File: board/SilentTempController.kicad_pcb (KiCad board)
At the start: 2 copper layers, 100 x 100 mm, 93 parts, among them J1 Barrel_Jack_Switch, J10 Conn_01x02_Pin, J11 Conn_01x02_Pin, J12 Screw_Terminal_01x02, J13 Screw_Terminal_01x02, J14 Screw_Terminal_01x02, J15 Screw_Terminal_01x02, J2 Screw_Terminal_01x02, J3 Conn_01x02_Pin, J4 Screw_Terminal_01x02, J5 Conn_01x02_Pin, J6 Screw_Terminal_01x02, J7 Conn_01x02_Pin, J8 Screw_Terminal_01x02, J9 Conn_01x02_Pin, Q1 2N3904, Q10 2N3904, Q11 2N3906, Q12 IRLZ44N, Q13 2N3904, Q14 2N3904, Q15 2N3906, Q16 IRLZ44N, Q17 2N3904, Q2 2N3906, Q3 IRLZ44N, Q4 2N3904, Q5 2N3904, Q6 2N3904, Q7 2N3906, Q8 IRLZ44N, Q9 2N3904, SW1 SW_Push, SW2 SW_Push, SW3 SW_Push, SW4 SW_Push, SW5 SW_Push, U1 LM7805_TO220

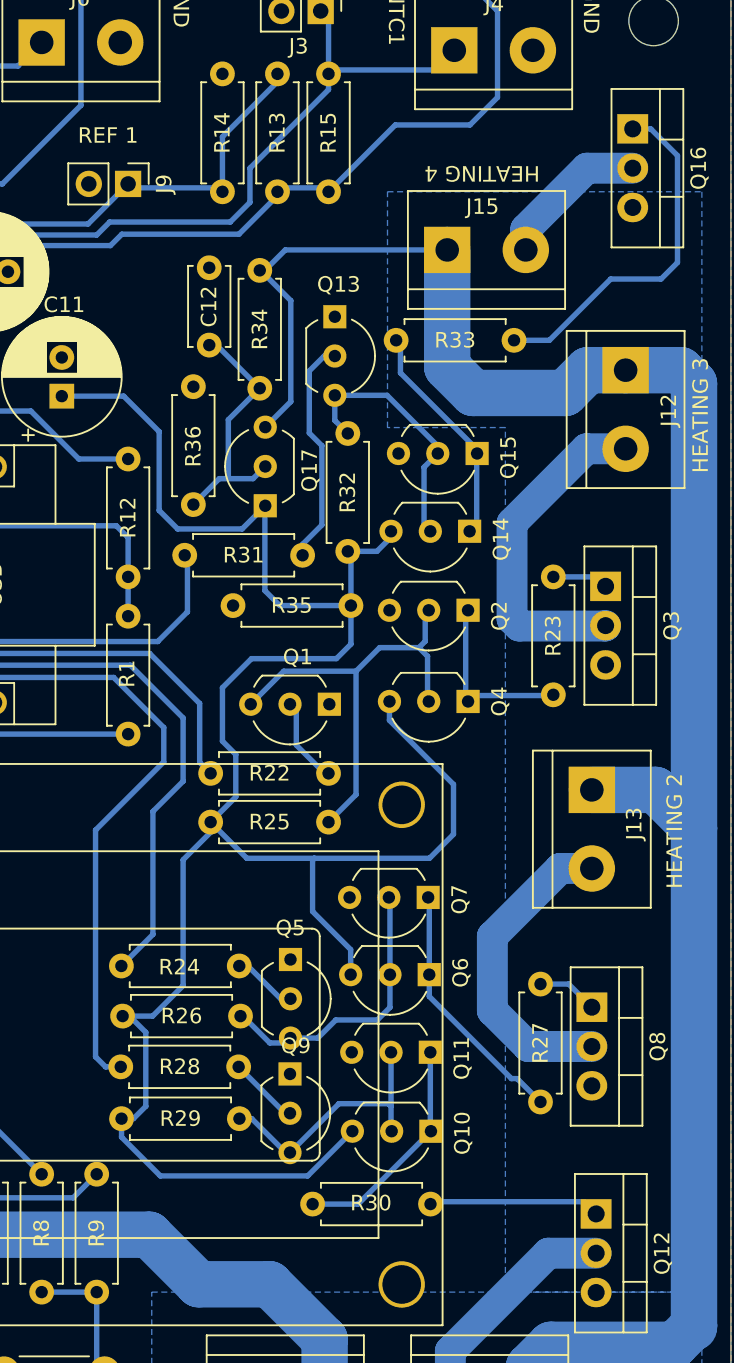
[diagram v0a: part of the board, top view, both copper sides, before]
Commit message: Added snubbers
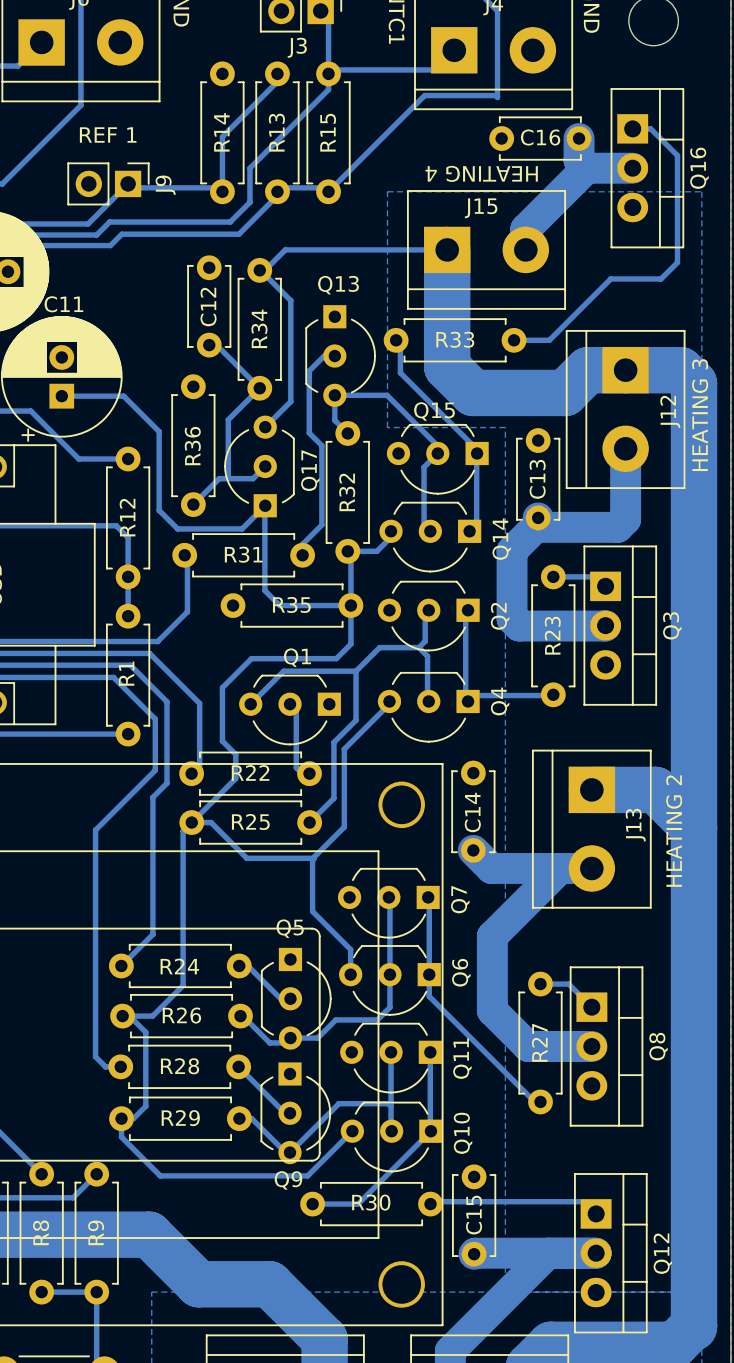
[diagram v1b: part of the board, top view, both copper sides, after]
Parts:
- added C13: 1000 nF, Capacitor_THT:C_Disc_D5.0mm_W2.5mm_P5.00mm, F.Cu at (187.5, 87.1)
- added C14: 1000 nF, Capacitor_THT:C_Disc_D5.0mm_W2.5mm_P5.00mm, F.Cu at (183.3, 108.6)
- added C15: 1000 nF, Capacitor_THT:C_Disc_D5.0mm_W2.5mm_P5.00mm, F.Cu at (183.4, 134.7)
- added C16: 1000 nF, Capacitor_THT:C_Disc_D5.0mm_W2.5mm_P5.00mm, F.Cu at (190.2, 62.6)
- moved R22 1.23 mm to (172.8, 103.7)
- moved R25 1.22 mm to (165.2, 106.8)
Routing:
- net Net-(J13-Pin_2): track 20.4 -> 28.6 mm
- net Net-(J14-Pin_2): track 14.8 -> 22.8 mm
- net +12V: track 140.0 -> 133.4 mm
- net Net-(J12-Pin_2): track 21.8 -> 24.1 mm
- net Net-(J15-Pin_2): track 9.89 -> 12.0 mm
- net /OC1B: track 37.4 -> 36.5 mm
- net Net-(Q1-C): track 29.3 -> 29.8 mm

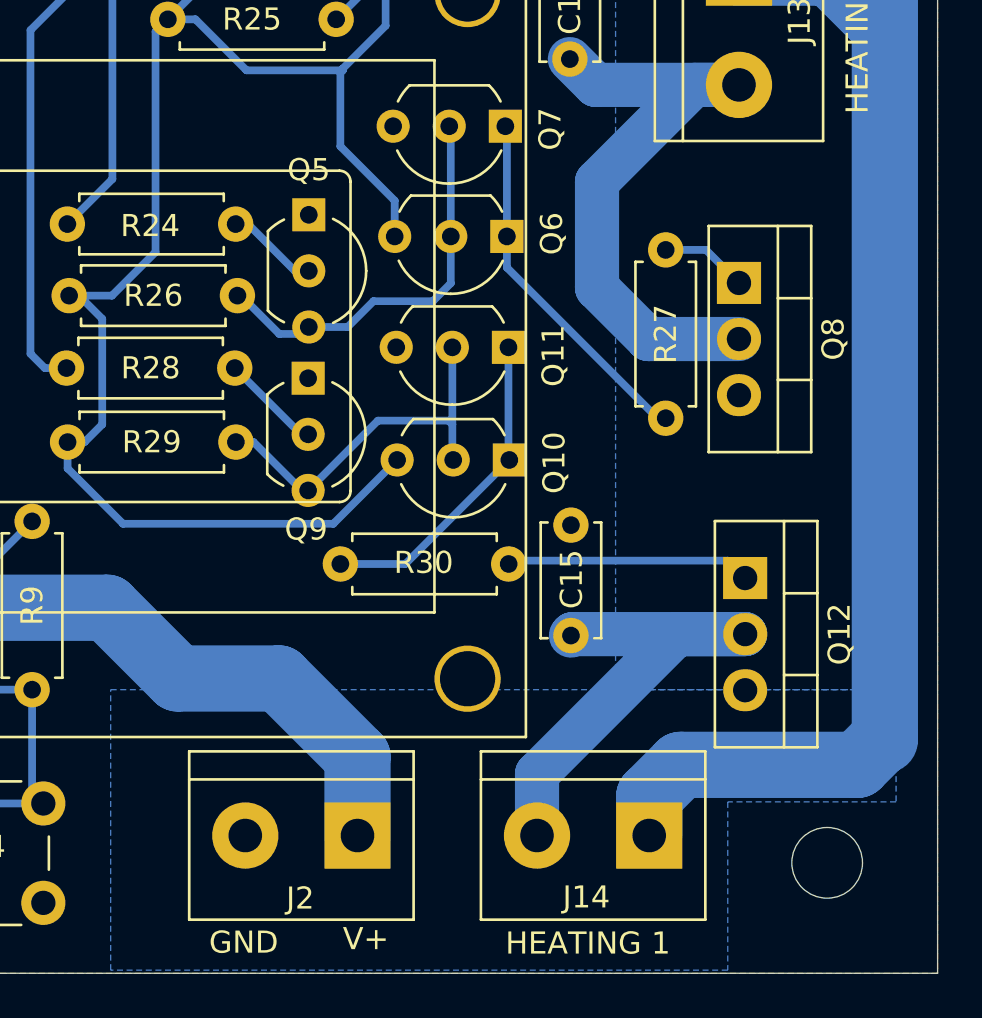
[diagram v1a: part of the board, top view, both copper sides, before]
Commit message: moved connectors
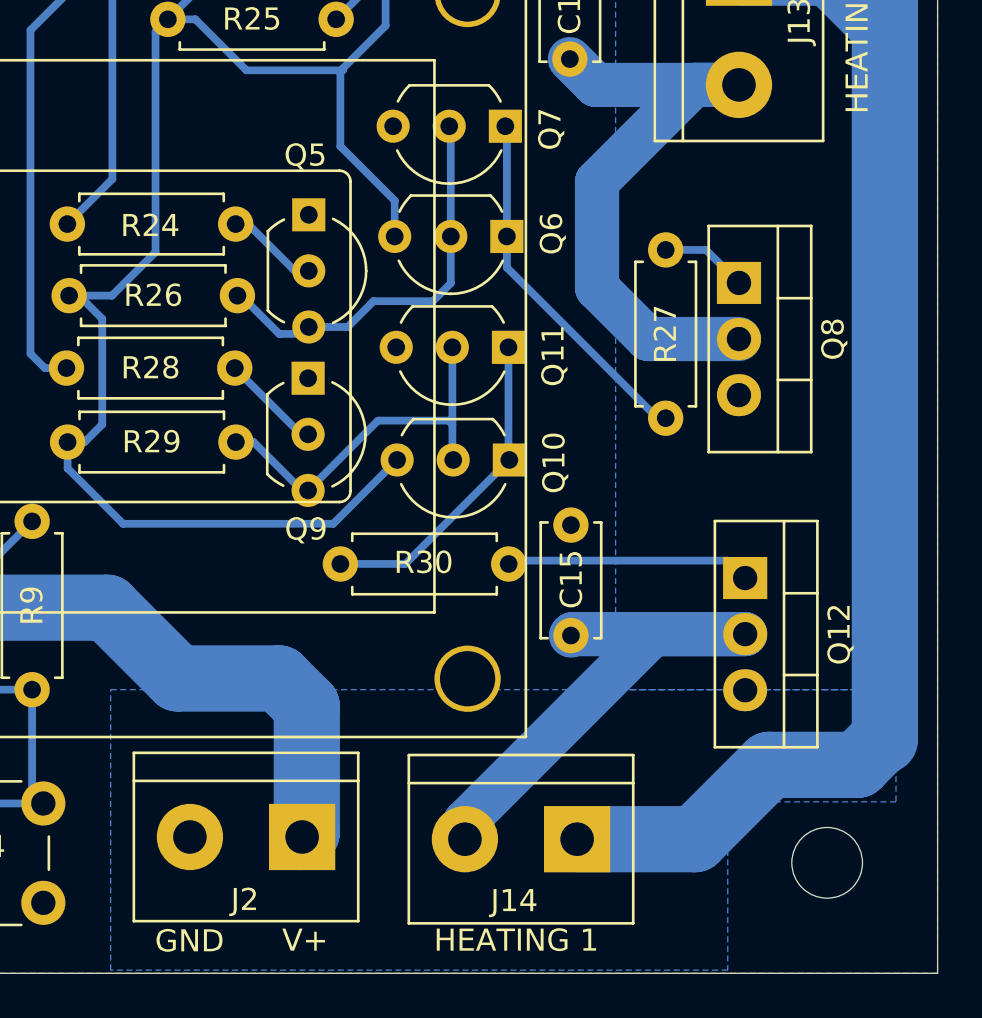
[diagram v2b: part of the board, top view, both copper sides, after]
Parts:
- moved J14 3.27 mm to (183.7, 143.9)
- moved J2 2.51 mm to (171.2, 143.8)
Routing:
- net Net-(J14-Pin_2): track 22.8 -> 24.9 mm
- net +24V: track 266.2 -> 267.7 mm
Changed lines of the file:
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@@
     (property "ki_keywords" "NPN Transistor")
     (attr through_hole)
-    (fp_text reference "Q5" (at -2.032 0 -180) (layer "F.SilkS")
+    (fp_text reference "Q5" (at -2.69 0.15 -180) (layer "F.SilkS")
         (effects (font (size 1 1) (thickness 0.15)))
     )
@@
   )
   (footprint "TerminalBlock:TerminalBlock_bornier-2_P5.08mm" (layer "F.Cu")
-    (at 173.736 143.764 180)
+    (at 171.23 143.83 180)
     (descr "simple 2-pin terminal block, pitch 5.08mm, revamped version of bornier2")
     (tags "terminal block bornier2")
@@
   )
   (footprint "TerminalBlock:TerminalBlock_bornier-2_P5.08mm" (layer "F.Cu")
-    (at 186.944 143.764 180)
+    (at 183.68 143.93 180)
     (descr "simple 2-pin terminal block, pitch 5.08mm, revamped version of bornier2")
     (tags "terminal block bornier2")
@@
     (effects (font (size 1 1) (thickness 0.15)) (justify left bottom))
   )
-  (gr_text "HEATING 1" (at 180.43 149.23) (layer "F.SilkS")
+  (gr_text "HEATING 1" (at 177.19 149.1) (layer "F.SilkS")
     (effects (font (size 1 1) (thickness 0.15)) (justify left bottom))
   )
@@
     (effects (font (size 1 1) (thickness 0.15)) (justify left bottom))
   )
-  (gr_text "V+" (at 173.07 149.03) (layer "F.SilkS")
+  (gr_text "V+" (at 170.32 149.1) (layer "F.SilkS")
     (effects (font (size 1 1) (thickness 0.15)) (justify left bottom))
   )
@@
     (effects (font (size 1 1) (thickness 0.15)) (justify left bottom))
   )
-  (gr_text "GND" (at 167.01 149.19) (layer "F.SilkS")
+  (gr_text "GND" (at 164.56 149.13) (layer "F.SilkS")
     (effects (font (size 1 1) (thickness 0.15)) (justify left bottom))
   )
@@
   (segment (start 184.58 114.16) (end 188.9612 109.7788) (width 2) (layer "B.Cu") (net 43))
   (segment (start 183.4646 134.6454) (end 183.4 134.71) (width 2) (layer "B.Cu") (net 44))
-  (segment (start 191.2874 134.6454) (end 188.1886 134.6454) (width 2) (layer "B.Cu") (net 44))
+  (segment (start 178.6 143.16) (end 178.6 143.93) (width 2) (layer "B.Cu") (net 44))
+  (segment (start 191.2874 134.6454) (end 187.1146 134.6454) (width 2) (layer "B.Cu") (net 44))
   (segment (start 191.2874 134.6454) (end 183.4646 134.6454) (width 2) (layer "B.Cu") (net 44))
-  (segment (start 188.1886 134.6454) (end 181.864 140.97) (width 2) (layer "B.Cu") (net 44))
-  (segment (start 181.864 140.97) (end 181.864 143.764) (width 2) (layer "B.Cu") (net 44))
+  (segment (start 187.1146 134.6454) (end 178.6 143.16) (width 2) (layer "B.Cu") (net 44))
   (segment (start 190.6778 64.516) (end 186.7408 68.453) (width 2) (layer "B.Cu") (net 45))
   (segment (start 186.7408 68.453) (end 186.7408 69.7992) (width 2) (layer "B.Cu") (net 45))
@@
   (segment (start 185.9788 75.6412) (end 188.2648 75.6412) (width 0.35) (layer "B.Cu") (net 57))
   (segment (start 196.5452 70.612) (end 196.5452 63.7032) (width 0.35) (layer "B.Cu") (net 57))
-  (segment (start 162.4 133.45) (end 112.622 133.45) (width 3) (layer "B.Cu") (net 58))
+  (segment (start 112.622 133.45) (end 103.05 123.878) (width 3) (layer "B.Cu") (net 58))
+  (segment (start 171.44 143.62) (end 171.44 137.912) (width 3) (layer "B.Cu") (net 58))
+  (segment (start 171.23 143.83) (end 171.44 143.62) (width 3) (layer "B.Cu") (net 58))
+  (segment (start 170.18 136.652) (end 165.602 136.652) (width 3) (layer "B.Cu") (net 58))
   (segment (start 197.612 107.188) (end 197.612 139.319) (width 3) (layer "B.Cu") (net 58))
   (segment (start 181.6608 77.3684) (end 181.6608 69.7992) (width 3) (layer "B.Cu") (net 58))
-  (segment (start 173.736 143.764) (end 173.736 140.208) (width 3) (layer "B.Cu") (net 58))
   (segment (start 110.5154 91.9988) (end 106.6292 91.9988) (width 3) (layer "B.Cu") (net 58))
   (segment (start 112.1918 81.3562) (end 112.1918 78.232) (width 3) (layer "B.Cu") (net 58))
-  (segment (start 186.944 141.986) (end 188.3664 140.5636) (width 3) (layer "B.Cu") (net 58))
+  (segment (start 183.68 143.93) (end 189.01 143.93) (width 3) (layer "B.Cu") (net 58))
   (segment (start 171.196 69.7992) (end 181.6608 69.7992) (width 0.35) (layer "B.Cu") (net 58))
-  (segment (start 196.3674 140.5636) (end 197.612 139.319) (width 3) (layer "B.Cu") (net 58))
-  (segment (start 112.622 133.45) (end 103.05 123.878) (width 3) (layer "B.Cu") (net 58))
-  (segment (start 188.3664 140.5636) (end 196.3674 140.5636) (width 3) (layer "B.Cu") (net 58))
+  (segment (start 162.4 133.45) (end 112.622 133.45) (width 3) (layer "B.Cu") (net 58))
+  (segment (start 192.3764 140.5636) (end 196.3674 140.5636) (width 3) (layer "B.Cu") (net 58))
   (segment (start 110.236 83.312) (end 112.776 85.852) (width 3) (layer "B.Cu") (net 58))
   (segment (start 171.5516 73.0758) (end 171.5516 79.6036) (width 0.35) (layer "B.Cu") (net 58))
   (segment (start 197.612 78.4352) (end 196.7484 77.5716) (width 3) (layer "B.Cu") (net 58))
-  (segment (start 186.944 143.764) (end 186.944 141.986) (width 3) (layer "B.Cu") (net 58))
   (segment (start 197.612 139.319) (end 197.612 139.446) (width 3) (layer "B.Cu") (net 58))
   (segment (start 169.545 71.12) (end 169.8752 71.12) (width 0.35) (layer "B.Cu") (net 58))
   (segment (start 193.1924 77.5716) (end 190.754 77.5716) (width 3) (layer "B.Cu") (net 58))
+  (segment (start 165.602 136.652) (end 162.4 133.45) (width 3) (layer "B.Cu") (net 58))
   (segment (start 106.6292 91.9988) (end 103.124 95.504) (width 3) (layer "B.Cu") (net 58))
   (segment (start 183.3372 79.0448) (end 181.6608 77.3684) (width 3) (layer "B.Cu") (net 58))
   (segment (start 169.5958 71.12) (end 171.5516 73.0758) (width 0.35) (layer "B.Cu") (net 58))
+  (segment (start 196.3674 140.5636) (end 197.612 139.319) (width 3) (layer "B.Cu") (net 58))
   (segment (start 169.545 71.12) (end 169.5958 71.12) (width 0.35) (layer "B.Cu") (net 58))
   (segment (start 115.316 78.232) (end 112.1918 78.232) (width 2) (layer "B.Cu") (net 58))
-  (segment (start 170.18 136.652) (end 165.602 136.652) (width 3) (layer "B.Cu") (net 58))
   (segment (start 195.1228 104.6988) (end 191.008 104.6988) (width 3) (layer "B.Cu") (net 58))
   (segment (start 197.612 107.188) (end 195.1228 104.6988) (width 3) (layer "B.Cu") (net 58))
-  (segment (start 173.736 140.208) (end 170.18 136.652) (width 3) (layer "B.Cu") (net 58))
+  (segment (start 103.05 123.878) (end 103.05 111.57) (width 3) (layer "B.Cu") (net 58))
   (segment (start 171.5516 79.6036) (end 169.9006 81.2546) (width 0.35) (layer "B.Cu") (net 58))
   (segment (start 189.2808 79.0448) (end 183.3372 79.0448) (width 3) (layer "B.Cu") (net 58))
+  (segment (start 171.44 137.912) (end 170.18 136.652) (width 3) (layer "B.Cu") (net 58))
   (segment (start 103.362 101.092) (end 103.124 101.092) (width 1.5) (layer "B.Cu") (net 58))
   (segment (start 110.236 83.312) (end 112.1918 81.3562) (width 3) (layer "B.Cu") (net 58))
   (segment (start 196.7484 77.5716) (end 193.1924 77.5716) (width 3) (layer "B.Cu") (net 58))
-  (segment (start 103.05 123.878) (end 103.05 111.57) (width 3) (layer "B.Cu") (net 58))
+  (segment (start 189.01 143.93) (end 192.3764 140.5636) (width 3) (layer "B.Cu") (net 58))
   (segment (start 112.1918 78.232) (end 107.3912 73.4314) (width 2) (layer "B.Cu") (net 58))
   (segment (start 112.776 85.852) (end 112.776 89.7382) (width 3) (layer "B.Cu") (net 58))
-  (segment (start 165.602 136.652) (end 162.4 133.45) (width 3) (layer "B.Cu") (net 58))
   (segment (start 197.612 107.188) (end 197.612 78.4352) (width 3) (layer "B.Cu") (net 58))
   (segment (start 169.8752 71.12) (end 171.196 69.7992) (width 0.35) (layer "B.Cu") (net 58))
